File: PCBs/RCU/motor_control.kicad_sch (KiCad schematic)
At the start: 18 parts

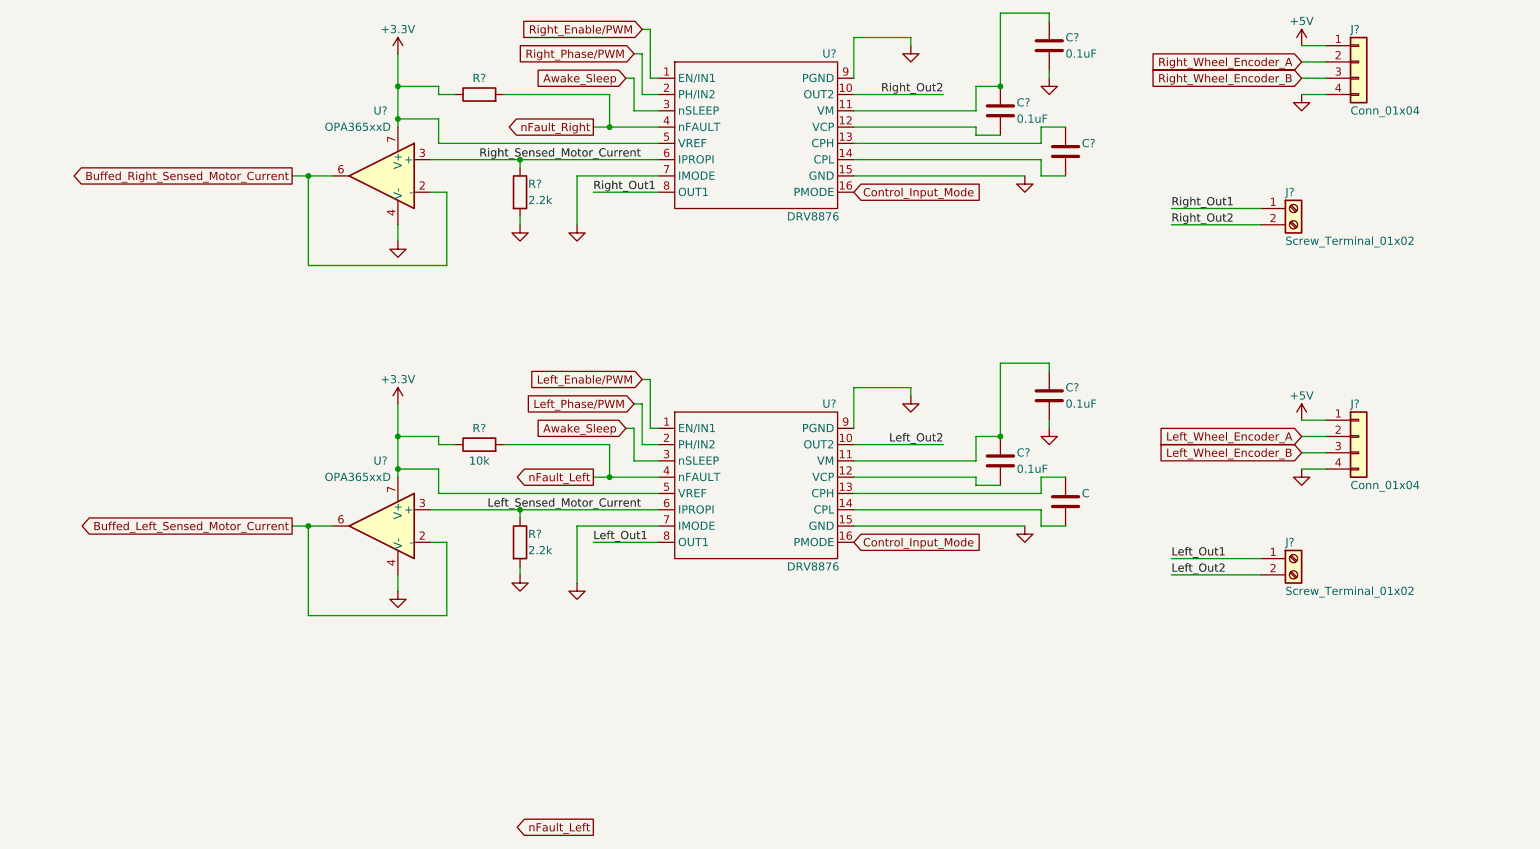
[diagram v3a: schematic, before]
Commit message: Numbered and ordered all of the modules
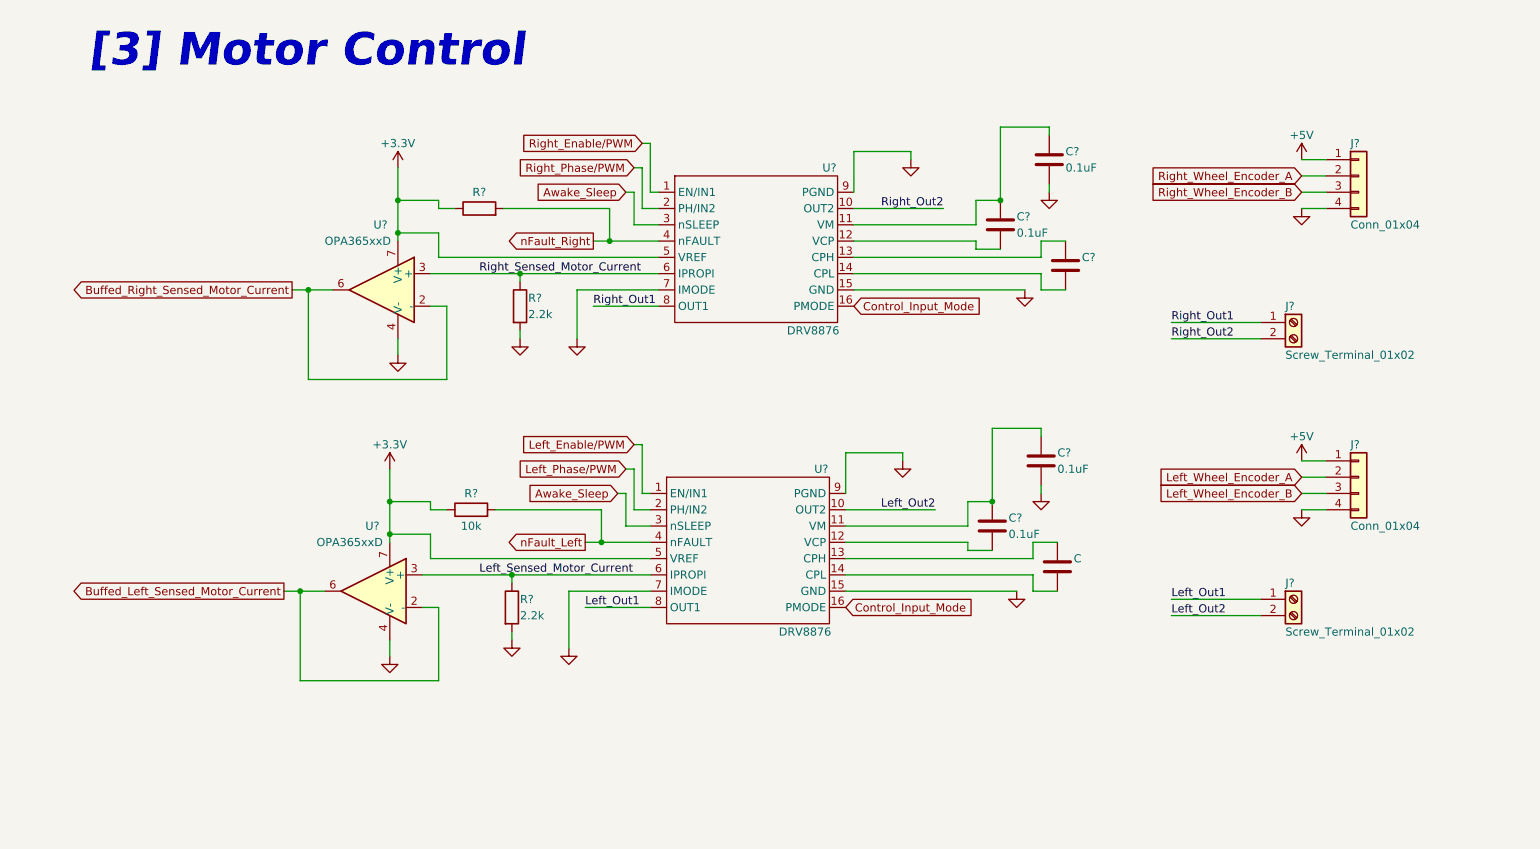
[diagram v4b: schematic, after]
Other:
- note added: "[3] Motor Control"
- moved on the sheet: C, C?, J?, R?, U?

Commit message: Annotated all components in motor control
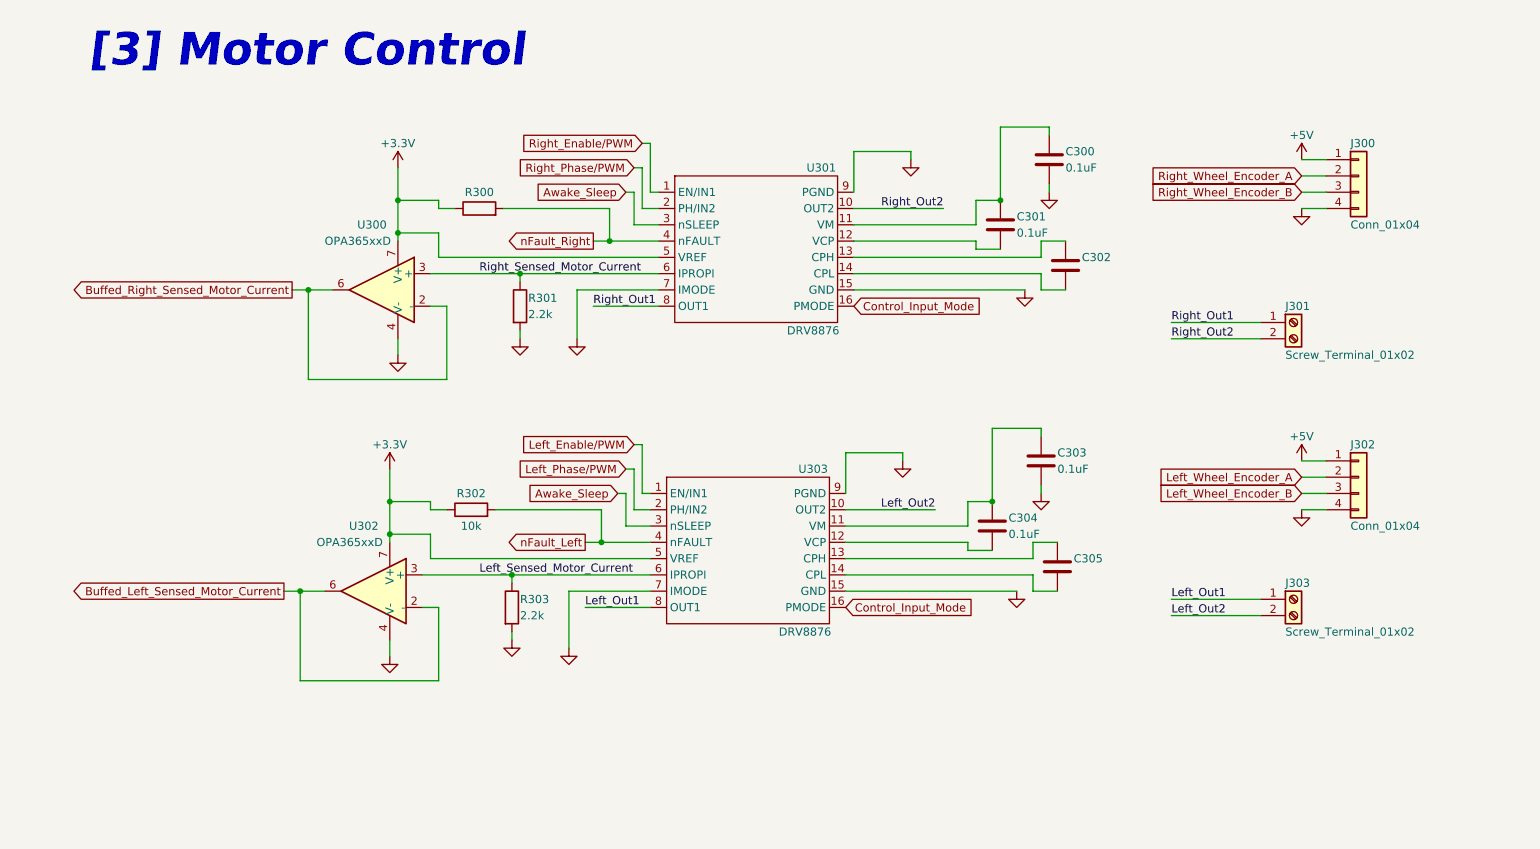
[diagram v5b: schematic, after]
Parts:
- gave numbers to parts that had none: 17
- renumbered C to C305
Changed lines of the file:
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@@
   (symbol (lib_id "Device:R") (at 83.82 110.49 0) (unit 1)
     (in_bom yes) (on_board yes)
-    (property "Reference" "R?" (id 0) (at 85.09 109.22 0)
+    (property "Reference" "R303" (id 0) (at 85.09 109.22 0)
       (effects (font (size 1.27 1.27)) (justify left))
     )
@@
   (symbol (lib_id "Ghanis_Symbols_KiCad6:DRV8876") (at 121.92 53.34 0) (unit 1)
     (in_bom yes) (on_board yes)
-    (property "Reference" "U?" (id 0) (at 133.35 41.91 0))
+    (property "Reference" "U301" (id 0) (at 132.08 41.91 0))
     (property "Value" "DRV8876" (id 1) (at 130.81 67.31 0))
     (property "Footprint" "" (id 2) (at 121.92 53.34 0)
@@
   (symbol (lib_id "Device:C") (at 160.02 50.8 0) (unit 1)
     (in_bom yes) (on_board yes)
-    (property "Reference" "C?" (id 0) (at 162.56 49.53 0)
+    (property "Reference" "C301" (id 0) (at 162.56 49.53 0)
       (effects (font (size 1.27 1.27)) (justify left))
     )
@@
   (symbol (lib_id "Connector:Screw_Terminal_01x02") (at 205.74 66.04 0) (unit 1)
     (in_bom yes) (on_board yes)
-    (property "Reference" "J?" (id 0) (at 204.47 63.5 0)
+    (property "Reference" "J301" (id 0) (at 204.47 63.5 0)
       (effects (font (size 1.27 1.27)) (justify left))
     )
@@
   (symbol (lib_id "Device:C") (at 167.64 40.64 0) (unit 1)
     (in_bom yes) (on_board yes)
-    (property "Reference" "C?" (id 0) (at 170.18 39.37 0)
+    (property "Reference" "C300" (id 0) (at 170.18 39.37 0)
       (effects (font (size 1.27 1.27)) (justify left))
     )
@@
   (symbol (lib_id "Device:R") (at 85.09 63.5 0) (unit 1)
     (in_bom yes) (on_board yes)
-    (property "Reference" "R?" (id 0) (at 86.36 62.23 0)
+    (property "Reference" "R301" (id 0) (at 86.36 62.23 0)
       (effects (font (size 1.27 1.27)) (justify left))
     )
@@
   (symbol (lib_id "Connector_Generic:Conn_01x04") (at 215.9 43.18 0) (unit 1)
     (in_bom yes) (on_board yes)
-    (property "Reference" "J?" (id 0) (at 214.63 38.1 0)
+    (property "Reference" "J300" (id 0) (at 214.63 38.1 0)
       (effects (font (size 1.27 1.27)) (justify left))
     )
@@
   (symbol (lib_id "Device:R") (at 78.74 48.26 90) (unit 1)
     (in_bom yes) (on_board yes)
-    (property "Reference" "R?" (id 0) (at 78.74 45.72 90))
+    (property "Reference" "R300" (id 0) (at 78.74 45.72 90))
     (property "Value" "" (id 1) (at 78.74 50.8 90))
     (property "Footprint" "" (id 2) (at 78.74 50.038 90)
@@
   (symbol (lib_id "Device:C") (at 170.18 57.15 0) (unit 1)
     (in_bom yes) (on_board yes)
-    (property "Reference" "C?" (id 0) (at 172.72 55.88 0)
+    (property "Reference" "C302" (id 0) (at 172.72 55.88 0)
       (effects (font (size 1.27 1.27)) (justify left))
     )
@@
   (symbol (lib_id "Amplifier_Operational:OPA365xxD") (at 63.5 60.96 0) (mirror y) (unit 1)
     (in_bom yes) (on_board yes)
-    (property "Reference" "U?" (id 0) (at 62.23 50.8 0)
+    (property "Reference" "U300" (id 0) (at 59.69 50.8 0)
       (effects (font (size 1.27 1.27)) (justify right))
     )
@@
   (symbol (lib_id "Device:C") (at 168.91 104.14 0) (unit 1)
     (in_bom yes) (on_board yes)
-    (property "Reference" "C" (id 0) (at 171.45 102.87 0)
+    (property "Reference" "C305" (id 0) (at 171.45 102.87 0)
       (effects (font (size 1.27 1.27)) (justify left))
     )
@@
   (symbol (lib_id "Ghanis_Symbols_KiCad6:DRV8876") (at 120.65 100.33 0) (unit 1)
     (in_bom yes) (on_board yes)
-    (property "Reference" "U?" (id 0) (at 132.08 88.9 0))
+    (property "Reference" "U303" (id 0) (at 130.81 88.9 0))
     (property "Value" "DRV8876" (id 1) (at 129.54 114.3 0))
     (property "Footprint" "" (id 2) (at 120.65 100.33 0)
@@
   (symbol (lib_id "Device:C") (at 158.75 97.79 0) (unit 1)
     (in_bom yes) (on_board yes)
-    (property "Reference" "C?" (id 0) (at 161.29 96.52 0)
+    (property "Reference" "C304" (id 0) (at 161.29 96.52 0)
       (effects (font (size 1.27 1.27)) (justify left))
     )
@@
   (symbol (lib_id "Device:C") (at 166.37 87.63 0) (unit 1)
     (in_bom yes) (on_board yes)
-    (property "Reference" "C?" (id 0) (at 168.91 86.36 0)
+    (property "Reference" "C303" (id 0) (at 168.91 86.36 0)
       (effects (font (size 1.27 1.27)) (justify left))
     )
@@
   (symbol (lib_id "Connector_Generic:Conn_01x04") (at 215.9 90.17 0) (unit 1)
     (in_bom yes) (on_board yes)
-    (property "Reference" "J?" (id 0) (at 214.63 85.09 0)
+    (property "Reference" "J302" (id 0) (at 214.63 85.09 0)
       (effects (font (size 1.27 1.27)) (justify left))
     )
@@
   (symbol (lib_id "Amplifier_Operational:OPA365xxD") (at 62.23 107.95 0) (mirror y) (unit 1)
     (in_bom yes) (on_board yes)
-    (property "Reference" "U?" (id 0) (at 60.96 97.79 0)
+    (property "Reference" "U302" (id 0) (at 58.42 97.79 0)
       (effects (font (size 1.27 1.27)) (justify right))
     )
@@
   (symbol (lib_id "Device:R") (at 77.47 95.25 90) (unit 1)
     (in_bom yes) (on_board yes)
-    (property "Reference" "R?" (id 0) (at 77.47 92.71 90))
+    (property "Reference" "R302" (id 0) (at 77.47 92.71 90))
     (property "Value" "10k" (id 1) (at 77.47 97.79 90))
     (property "Footprint" "" (id 2) (at 77.47 97.028 90)
@@
   (symbol (lib_id "Connector:Screw_Terminal_01x02") (at 205.74 109.22 0) (unit 1)
     (in_bom yes) (on_board yes)
-    (property "Reference" "J?" (id 0) (at 204.47 106.68 0)
-      (effects (font (size 1.27 1.27)) (justify left))
-    )
+    (property "Reference" "J303" (id 0) (at 204.47 106.68 0)
+      (effects (font (size 1.27 1.27)) (justify left))
+    )

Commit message: Laballed sub-units of Motor Control
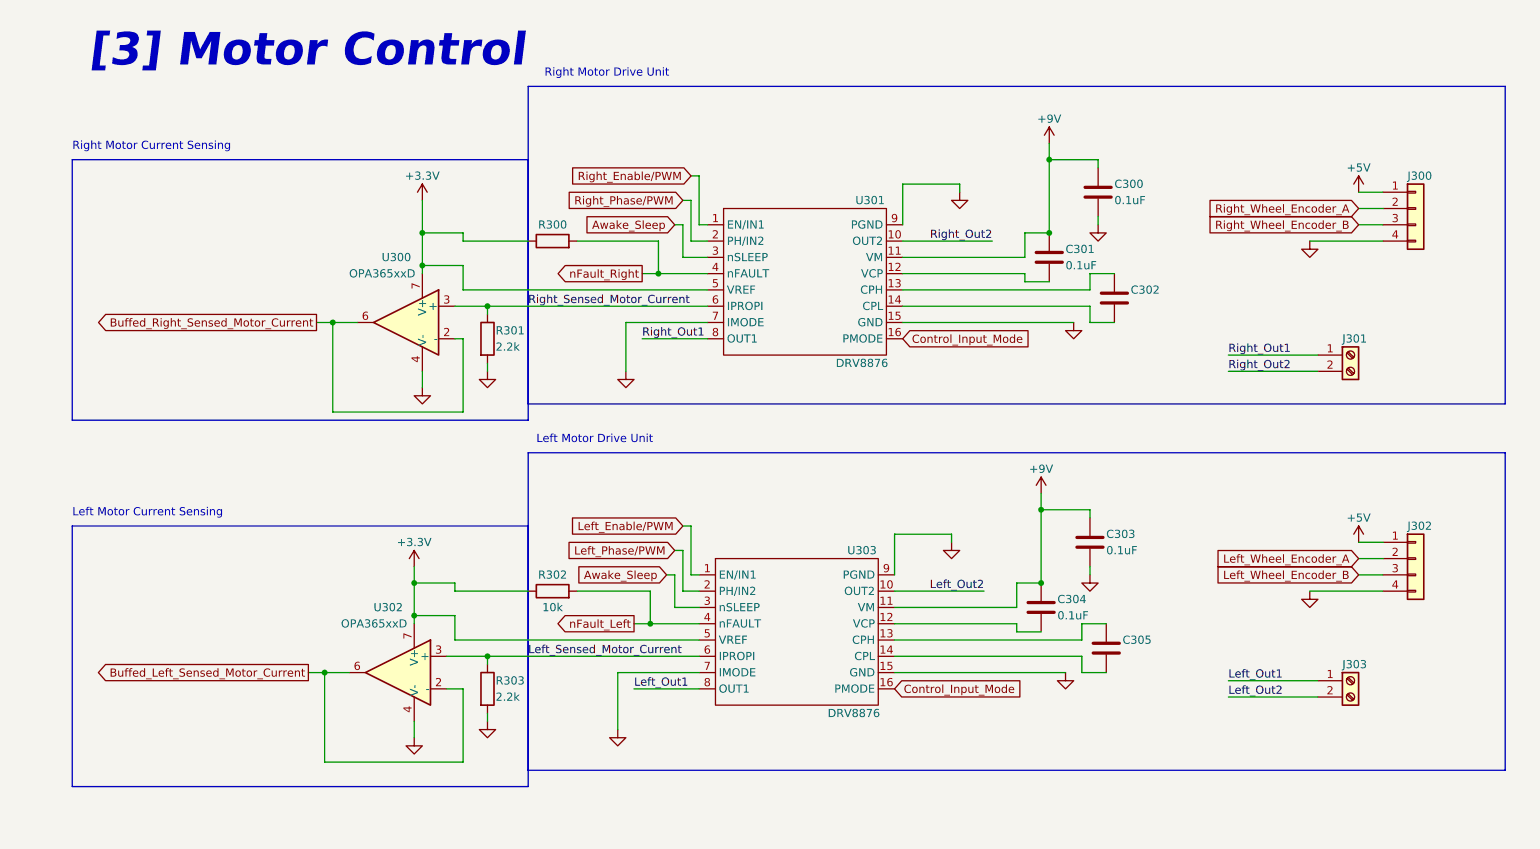
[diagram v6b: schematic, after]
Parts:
- J300, J302: value Conn_01x04 -> (none)
- J301, J303: value Screw_Terminal_01x02 -> (none)
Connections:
- net +9V: now reaches C300.1, C301.1, U301.11 (VM)
- net +9V: now also C303.1, C304.1, U303.11 (VM)
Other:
- note added: "Left Motor Current Sensing"
- note added: "Left Motor Drive Unit"
- note added: "Right Motor Current Sensing"
- note added: "Right Motor Drive Unit"
- moved on the sheet: C300, C301, C302, C303, C304, C305, J300, J301, J302, J303, R300, R301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
